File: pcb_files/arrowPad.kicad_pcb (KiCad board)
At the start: 2 copper layers, 90.2 x 90.2 mm, 65 parts, among them J1 AudioJack3_Ground, J2 AudioJack3_Ground, K1 KEYSW, K10 KEYSW, K11 KEYSW, K12 KEYSW, K13 KEYSW, K14 KEYSW, K15 KEYSW, K16 KEYSW, K2 KEYSW, K3 KEYSW, K4 KEYSW, K5 KEYSW, K6 KEYSW, K7 KEYSW, K8 KEYSW, K9 KEYSW, U1 ProMicro, U2 NRF24L01_Breakout, U3 ADG417BN, U4 AMS1117-3.3, U5 ADG417BN, U6 ADG417BN, U7 TLC5940PWP

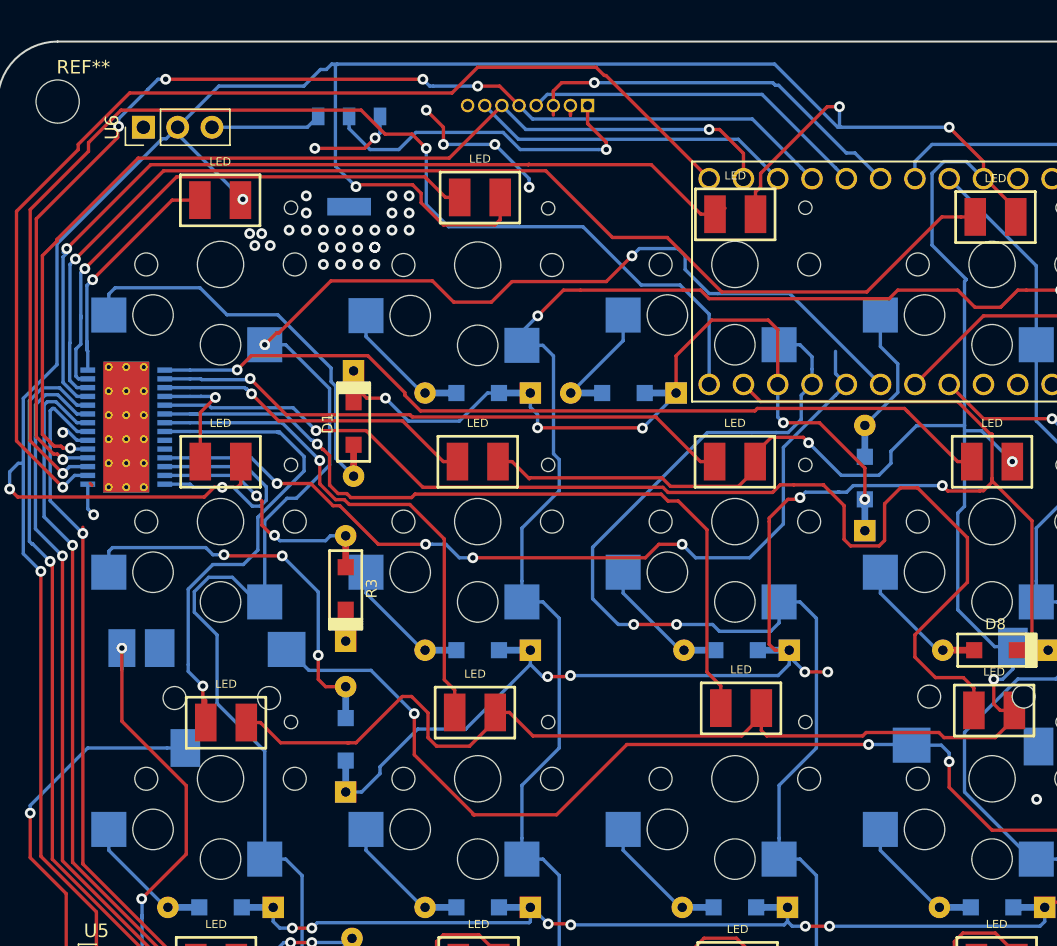
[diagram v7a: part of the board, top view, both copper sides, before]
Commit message: cleaned up traces
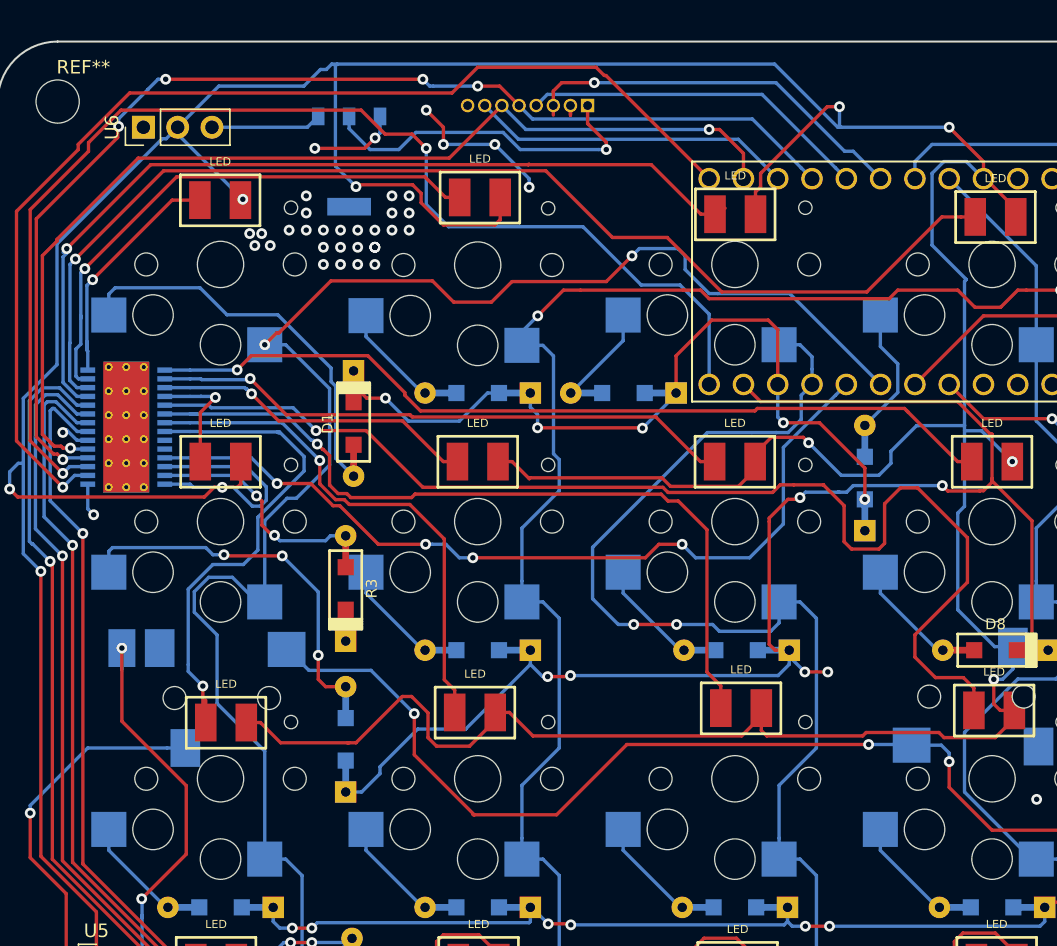
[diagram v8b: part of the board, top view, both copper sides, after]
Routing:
- net /GSCLK: track 65.8 -> 63.0 mm
